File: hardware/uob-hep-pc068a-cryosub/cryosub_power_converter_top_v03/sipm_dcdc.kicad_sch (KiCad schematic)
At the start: 20 parts, among them U3 MAX15059BATE+

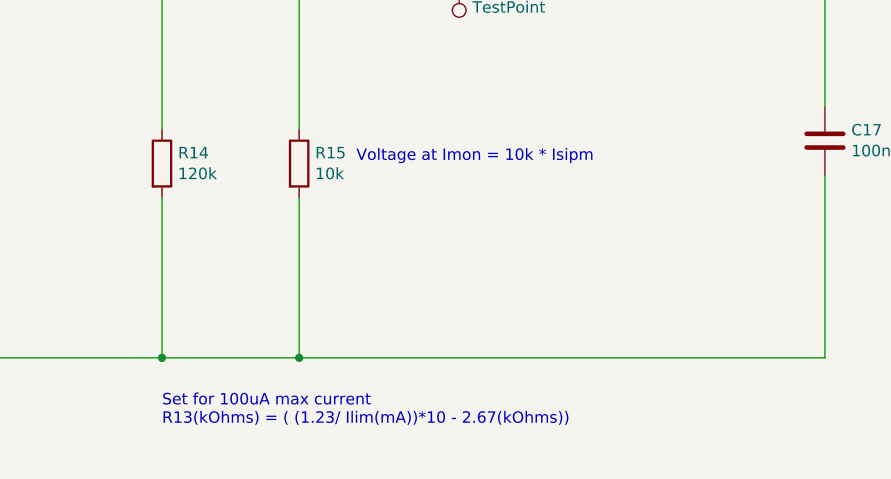
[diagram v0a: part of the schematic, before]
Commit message: Tweaked layout to remove DRCs (mainly silk) removed duplicate D1
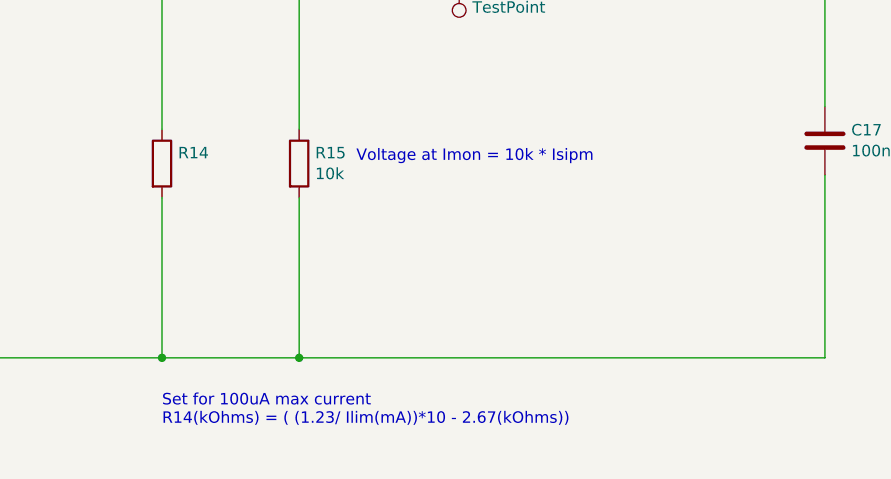
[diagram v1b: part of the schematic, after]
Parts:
- R14: value 120k -> (none); footprint Resistor_SMD:R_0402_1005Metric -> (none)
- R15, R17: footprint Resistor_SMD:R_0402_1005Metric -> (none)
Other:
- note added: "Set for 100uA max current R14(kOhms) = ( (1.23/ Ilim(mA))*10 - 2.67(kOhms))"
- note removed: "Set for 100uA max current R13(kOhms) = ( (1.23/ Ilim(mA))*10 - 2.67(kOhms))"
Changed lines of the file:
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@@
     (effects (font (size 1.27 1.27)) (justify left bottom))
   )
-  (text "Set for 100uA max current\nR13(kOhms) = ( (1.23/ Ilim(mA))*10 - 2.67(kOhms))"
+  (text "Set for 100uA max current\nR14(kOhms) = ( (1.23/ Ilim(mA))*10 - 2.67(kOhms))"
     (at 190.5 163.83 0)
     (effects (font (size 1.27 1.27)) (justify left bottom))
@@
       (effects (font (size 1.27 1.27)) (justify left))
     )
-    (property "Footprint" "Resistor_SMD:R_0402_1005Metric" (id 2) (at 212.852 81.28 90)
+    (property "Footprint" "" (id 2) (at 212.852 81.28 90)
       (effects (font (size 1.27 1.27)) hide)
     )
@@
       (effects (font (size 1.27 1.27)) (justify left))
     )
-    (property "Value" "120k" (id 1) (at 192.278 135.763 0)
-      (effects (font (size 1.27 1.27)) (justify left))
-    )
-    (property "Footprint" "Resistor_SMD:R_0402_1005Metric" (id 2) (at 188.722 134.62 90)
+    (property "Value" "" (id 1) (at 192.278 135.763 0)
+      (effects (font (size 1.27 1.27)) (justify left))
+    )
+    (property "Footprint" "" (id 2) (at 188.722 134.62 90)
       (effects (font (size 1.27 1.27)) hide)
     )
@@
       (effects (font (size 1.27 1.27)) (justify left))
     )
-    (property "Footprint" "Resistor_SMD:R_0402_1005Metric" (id 2) (at 203.962 134.62 90)
-      (effects (font (size 1.27 1.27)) hide)
-    )
+    (property "Footprint" "" (id 2) (at 203.962 134.62 90)
+      (effects (font (size 1.27 1.27)) hide)
+    )

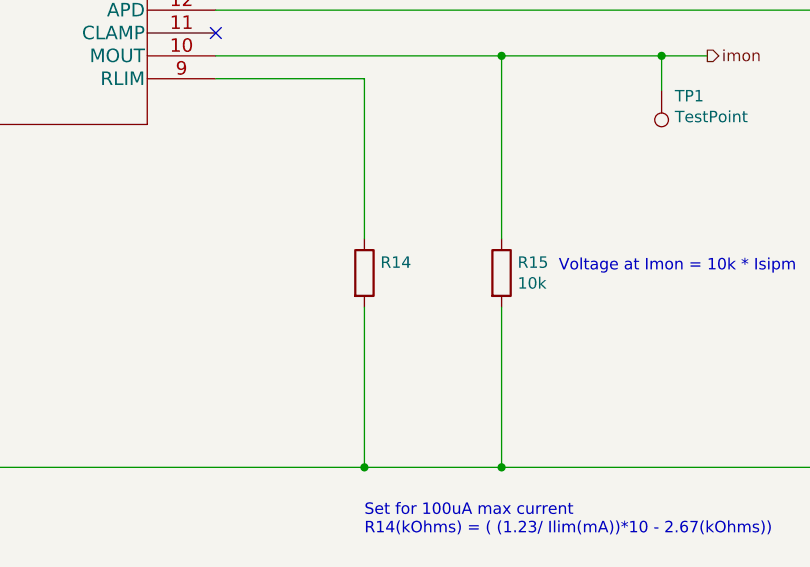
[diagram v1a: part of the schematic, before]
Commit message: Replacing FDD306 with SiS407
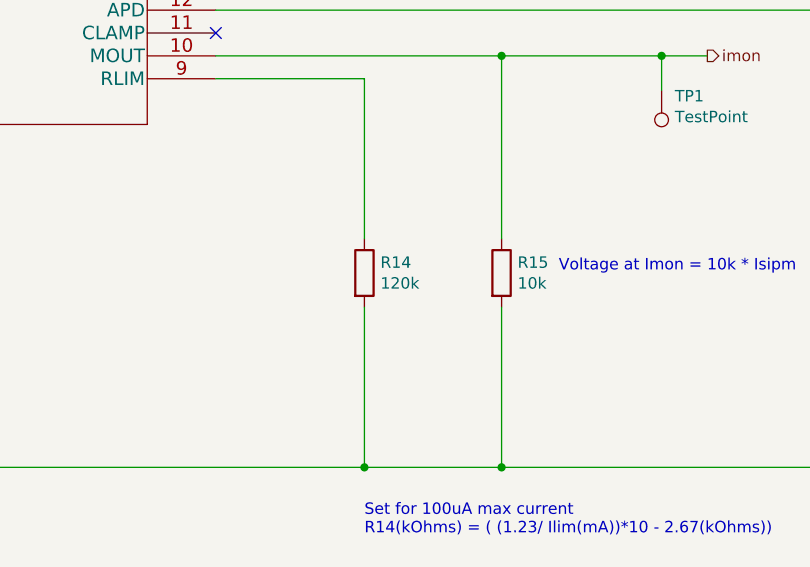
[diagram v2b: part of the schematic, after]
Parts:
- R14: value (none) -> 120k; footprint (none) -> Resistor_SMD:R_0603_1608Metric
- R15, R17: footprint (none) -> Resistor_SMD:R_0603_1608Metric
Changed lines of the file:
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@@
       (effects (font (size 1.27 1.27)) (justify left))
     )
-    (property "Footprint" "" (id 2) (at 212.852 81.28 90)
+    (property "Footprint" "Resistor_SMD:R_0603_1608Metric" (id 2) (at 212.852 81.28 90)
       (effects (font (size 1.27 1.27)) hide)
     )
@@
       (effects (font (size 1.27 1.27)) (justify left))
     )
-    (property "Value" "" (id 1) (at 192.278 135.763 0)
+    (property "Value" "120k" (id 1) (at 192.278 135.763 0)
       (effects (font (size 1.27 1.27)) (justify left))
     )
-    (property "Footprint" "" (id 2) (at 188.722 134.62 90)
+    (property "Footprint" "Resistor_SMD:R_0603_1608Metric" (id 2) (at 188.722 134.62 90)
       (effects (font (size 1.27 1.27)) hide)
     )
@@
       (effects (font (size 1.27 1.27)) (justify left))
     )
-    (property "Footprint" "" (id 2) (at 203.962 134.62 90)
+    (property "Footprint" "Resistor_SMD:R_0603_1608Metric" (id 2) (at 203.962 134.62 90)
       (effects (font (size 1.27 1.27)) hide)
     )
